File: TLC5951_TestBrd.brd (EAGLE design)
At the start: 50 x 55 mm, 9 parts, among them U3 V_REG_LDOSMD

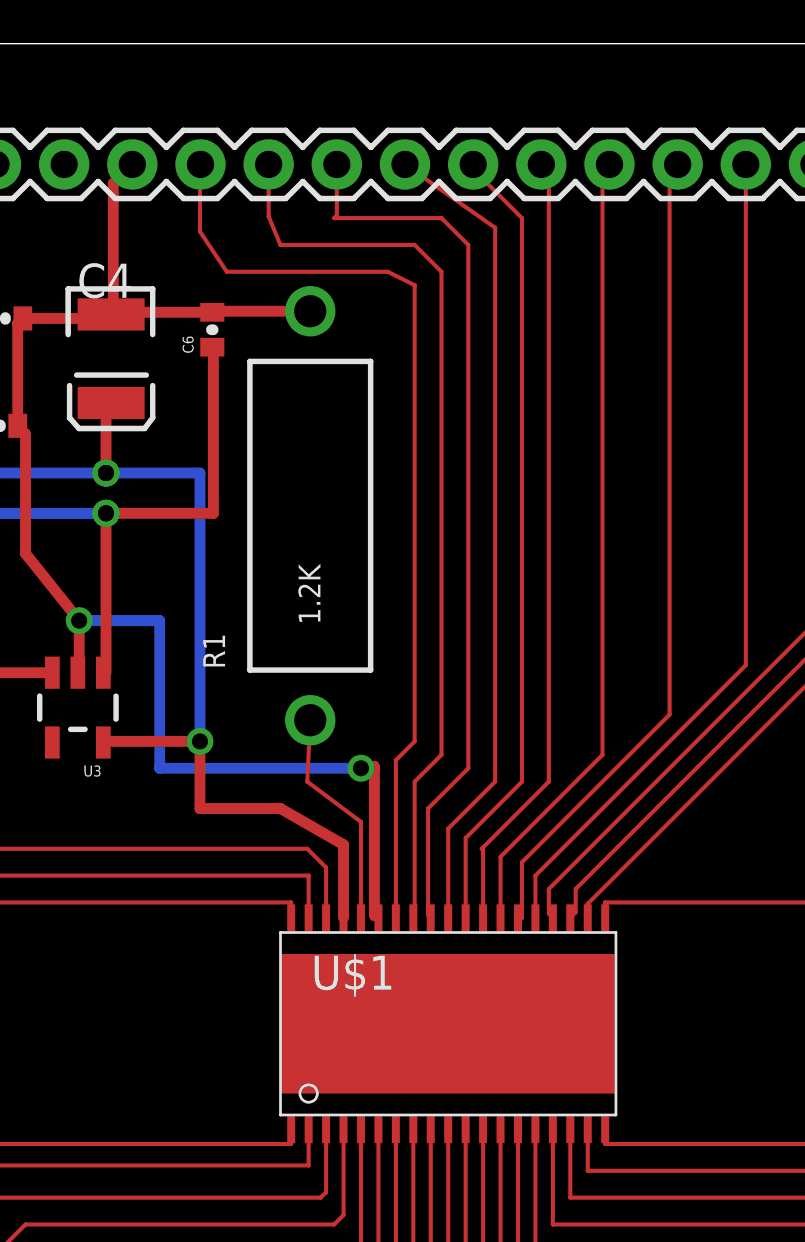
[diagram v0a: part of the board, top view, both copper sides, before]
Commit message: Corrected a few minor ommissions
1. Added three missing traces
2. Made trace to Vcc pin on chip thinner to avoid bridging two pins
3. The holes under the chip are now visible. Apparently I had not used
the updated library file!?
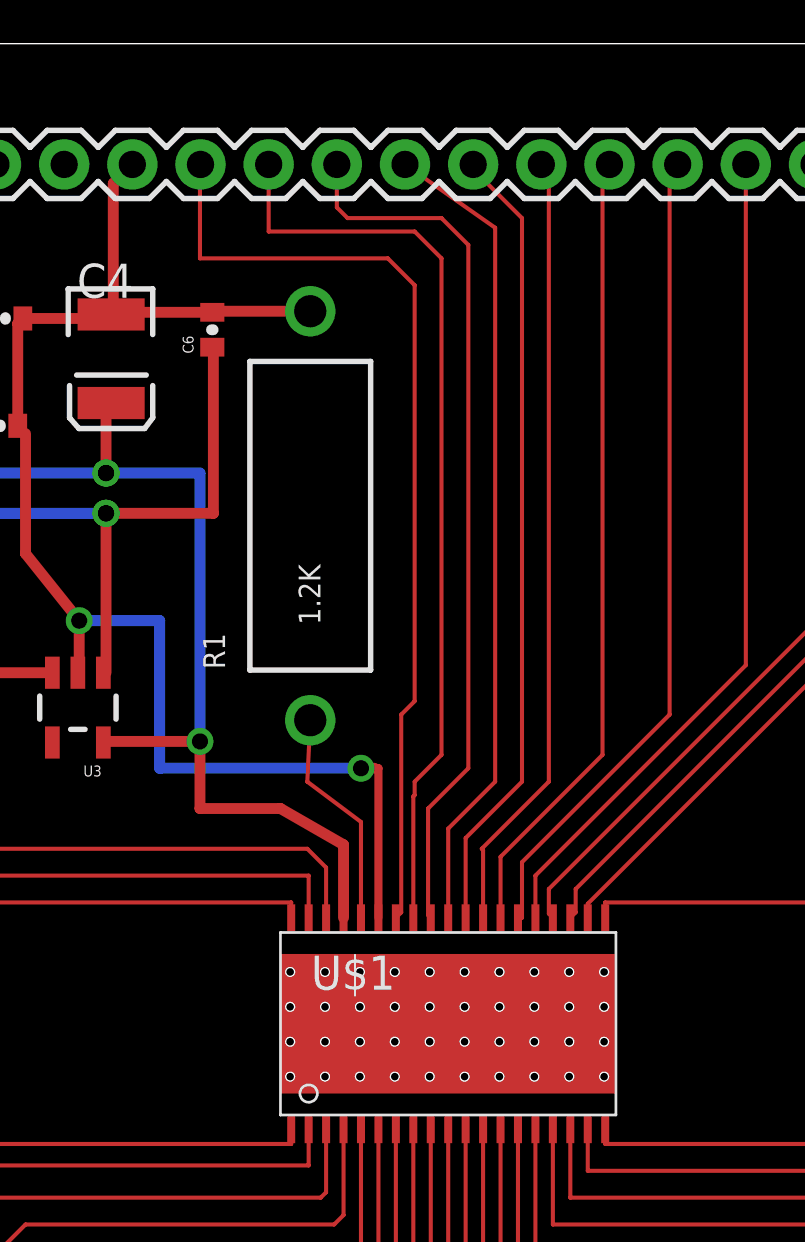
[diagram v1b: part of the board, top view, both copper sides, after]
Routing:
- net N$1: track 35.3 -> 35.8 mm
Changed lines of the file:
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@@
 <wire x1="24" y1="28" x2="23.5" y2="28" width="0.4064" layer="1"/>
 <wire x1="13" y1="33.5" x2="13" y2="31.5" width="0.4064" layer="1"/>
-<wire x1="12.95" y1="31.5601" x2="13" y2="31.5" width="0" layer="19" extent="1-1"/>
-<wire x1="24" y1="28.08" x2="24" y2="28" width="0" layer="19" extent="1-1"/>
 <wire x1="14.27" y1="44.99" x2="14.27" y2="49.79" width="0.4064" layer="1"/>
 <wire x1="14.27" y1="49.79" x2="14.98" y2="50.5" width="0.4064" layer="1"/>
-<wire x1="24" y1="28.08" x2="24" y2="22.5" width="0.4064" layer="1"/>
-<wire x1="24" y1="22.5" x2="24.15" y2="22.43" width="0" layer="19" extent="1-16"/>
+<wire x1="13" y1="31.5" x2="12.95" y2="31.5601" width="0" layer="19" extent="1-1"/>
+<wire x1="24" y1="28" x2="24.15" y2="28" width="0.3048" layer="1"/>
+<wire x1="24.15" y1="28" x2="24.15" y2="22.43" width="0.3048" layer="1"/>
 </signal>
 <signal name="GSSIN">
@@
 <wire x1="21.61" y1="29.79" x2="21.5" y2="27.5" width="0.1524" layer="1"/>
 </signal>
-<signal name="N$1">
-<contactref element="U$1" pad="32"/>
-<contactref element="PINS_20_38" pad="13"/>
-<wire x1="17.52" y1="50.5" x2="17.5" y2="50.48" width="0.1524" layer="1"/>
-<wire x1="17.5" y1="50.48" x2="17.5" y2="48" width="0.1524" layer="1"/>
-<wire x1="17.5" y1="48" x2="18.5" y2="46.5" width="0.1524" layer="1"/>
-<wire x1="18.5" y1="46.5" x2="24.5" y2="46.5" width="0.1524" layer="1"/>
-<wire x1="24.5" y1="46.5" x2="25.5" y2="46" width="0.1524" layer="1"/>
-<wire x1="25.5" y1="46" x2="25.5" y2="29" width="0.1524" layer="1"/>
-<wire x1="25.5" y1="29" x2="24.8" y2="28.3" width="0.1524" layer="1"/>
-<wire x1="24.8" y1="28.3" x2="24.8" y2="22.43" width="0.1524" layer="1"/>
-</signal>
-<signal name="N$3">
-<contactref element="U$1" pad="31"/>
-<contactref element="PINS_20_38" pad="12"/>
-<wire x1="26.5" y1="28.5" x2="25.5" y2="27.5" width="0.1524" layer="1"/>
-<wire x1="25.5" y1="27.5" x2="25.5" y2="22.48" width="0.1524" layer="1"/>
-<wire x1="25.5" y1="22.48" x2="25.45" y2="22.43" width="0.1524" layer="1"/>
-<wire x1="26.5" y1="28.5" x2="26.5" y2="46.5" width="0.1524" layer="1"/>
-<wire x1="26.5" y1="46.5" x2="25.5" y2="47.5" width="0.1524" layer="1"/>
-<wire x1="25.5" y1="47.5" x2="20.5" y2="47.5" width="0.1524" layer="1"/>
-<wire x1="20.5" y1="47.5" x2="20.06" y2="48.56" width="0.1524" layer="1"/>
-<wire x1="20.06" y1="48.56" x2="20.06" y2="50.5" width="0.1524" layer="1"/>
-</signal>
-<signal name="N$4">
-<contactref element="U$1" pad="30"/>
-<contactref element="PINS_20_38" pad="11"/>
-<wire x1="26.1" y1="22.43" x2="26" y2="22.53" width="0.1524" layer="1"/>
-<wire x1="26" y1="22.53" x2="26" y2="26.5" width="0.1524" layer="1"/>
-<wire x1="26" y1="26.5" x2="27.5" y2="28" width="0.1524" layer="1"/>
-<wire x1="27.5" y1="28" x2="27.5" y2="47.5" width="0.1524" layer="1"/>
-<wire x1="27.5" y1="47.5" x2="26.5" y2="48.5" width="0.1524" layer="1"/>
-<wire x1="26.5" y1="48.5" x2="22.5" y2="48.5" width="0.1524" layer="1"/>
-<wire x1="22.5" y1="48.5" x2="22.6" y2="48.6" width="0.1524" layer="1"/>
-<wire x1="22.6" y1="48.6" x2="22.6" y2="50.5" width="0.1524" layer="1"/>
-</signal>
 <signal name="N$5">
 <contactref element="U$1" pad="29"/>
@@
 <via x="9.5" y="39" extent="1-16" drill="0.6"/>
 </signal>
+<signal name="N$1">
+<contactref element="U$1" pad="32"/>
+<contactref element="PINS_20_38" pad="13"/>
+<wire x1="17.52" y1="50.5" x2="17.5" y2="50.5" width="0.254" layer="1"/>
+<wire x1="17.5" y1="50.5" x2="17.5" y2="47" width="0.1524" layer="1"/>
+<wire x1="17.5" y1="47" x2="24.5" y2="47" width="0.1524" layer="1"/>
+<wire x1="24.5" y1="47" x2="25.5" y2="46" width="0.1524" layer="1"/>
+<wire x1="25.5" y1="46" x2="25.5" y2="30.5" width="0.1524" layer="1"/>
+<wire x1="25.5" y1="30.5" x2="25" y2="30" width="0.1524" layer="1"/>
+<wire x1="25" y1="30" x2="25" y2="22.63" width="0.1524" layer="1"/>
+<wire x1="25" y1="22.63" x2="24.8" y2="22.43" width="0.1524" layer="1"/>
+</signal>
+<signal name="N$3">
+<contactref element="PINS_20_38" pad="12"/>
+<contactref element="U$1" pad="31"/>
+<wire x1="25.45" y1="22.43" x2="25.45" y2="26.95" width="0.1524" layer="1"/>
+<wire x1="25.45" y1="26.95" x2="25.5" y2="27" width="0.1524" layer="1"/>
+<wire x1="25.5" y1="27" x2="25.5" y2="27.5" width="0.1524" layer="1"/>
+<wire x1="25.5" y1="27.5" x2="26.5" y2="28.5" width="0.1524" layer="1"/>
+<wire x1="26.5" y1="28.5" x2="26.5" y2="47" width="0.1524" layer="1"/>
+<wire x1="26.5" y1="47" x2="25.5" y2="48" width="0.1524" layer="1"/>
+<wire x1="25.5" y1="48" x2="20.06" y2="48" width="0.1524" layer="1"/>
+<wire x1="20.06" y1="48" x2="20.06" y2="50.5" width="0.1524" layer="1"/>
+</signal>
+<signal name="N$4">
+<contactref element="U$1" pad="30"/>
+<contactref element="PINS_20_38" pad="11"/>
+<wire x1="22.6" y1="50.5" x2="22.6" y2="48.9" width="0.1524" layer="1"/>
+<wire x1="22.6" y1="48.9" x2="23" y2="48.5" width="0.1524" layer="1"/>
+<wire x1="23" y1="48.5" x2="26.5" y2="48.5" width="0.1524" layer="1"/>
+<wire x1="26.5" y1="48.5" x2="27.5" y2="47.5" width="0.1524" layer="1"/>
+<wire x1="27.5" y1="47.5" x2="27.5" y2="28" width="0.1524" layer="1"/>
+<wire x1="27.5" y1="28" x2="26" y2="26.5" width="0.1524" layer="1"/>
+<wire x1="26" y1="26.5" x2="26" y2="22.53" width="0.1524" layer="1"/>
+<wire x1="26" y1="22.53" x2="26.1" y2="22.43" width="0.1524" layer="1"/>
+</signal>
 </signals>
